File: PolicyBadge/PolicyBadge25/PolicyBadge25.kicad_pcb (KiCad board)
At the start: 2 copper layers, 193.3 x 122.1 mm, 70 parts, among them CN1 PH2.0-2P-LT, J1 Feed Point 915MHz, J2 Feed Point 2.4 GHz, Q1 2N7002, SW1 TA-3525-A1, U1 HS96L03W2C03, U10 YX-SMD5020, U11 IP2312-4V35, U2 MOUDLE-SEEEDUINO-XIAO-ESP32S3, U4 TPS613222ADBVR, U9 TCA9555PWR

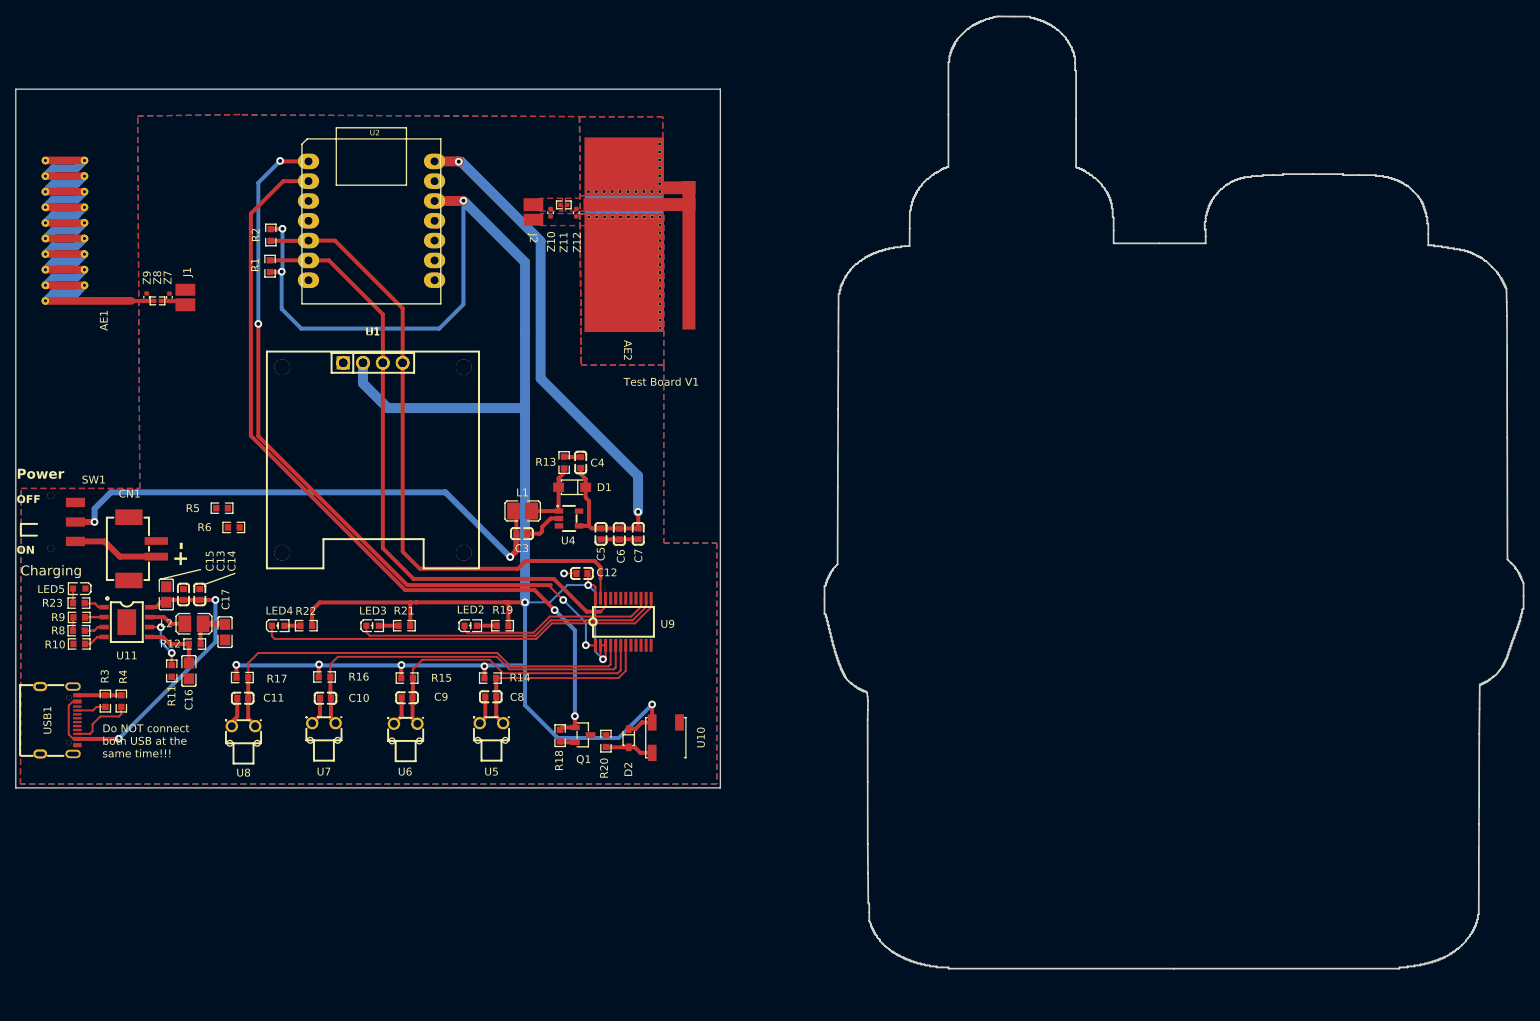
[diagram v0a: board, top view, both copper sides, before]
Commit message: Lots of changes, laying out board for board shape
Updated switches
Added headers for XAIO
Fixed Batt Connector polarity
10K pullup on int
Batt monitor resistor divider
Fix buzzer trace
XAIO footprint spacing
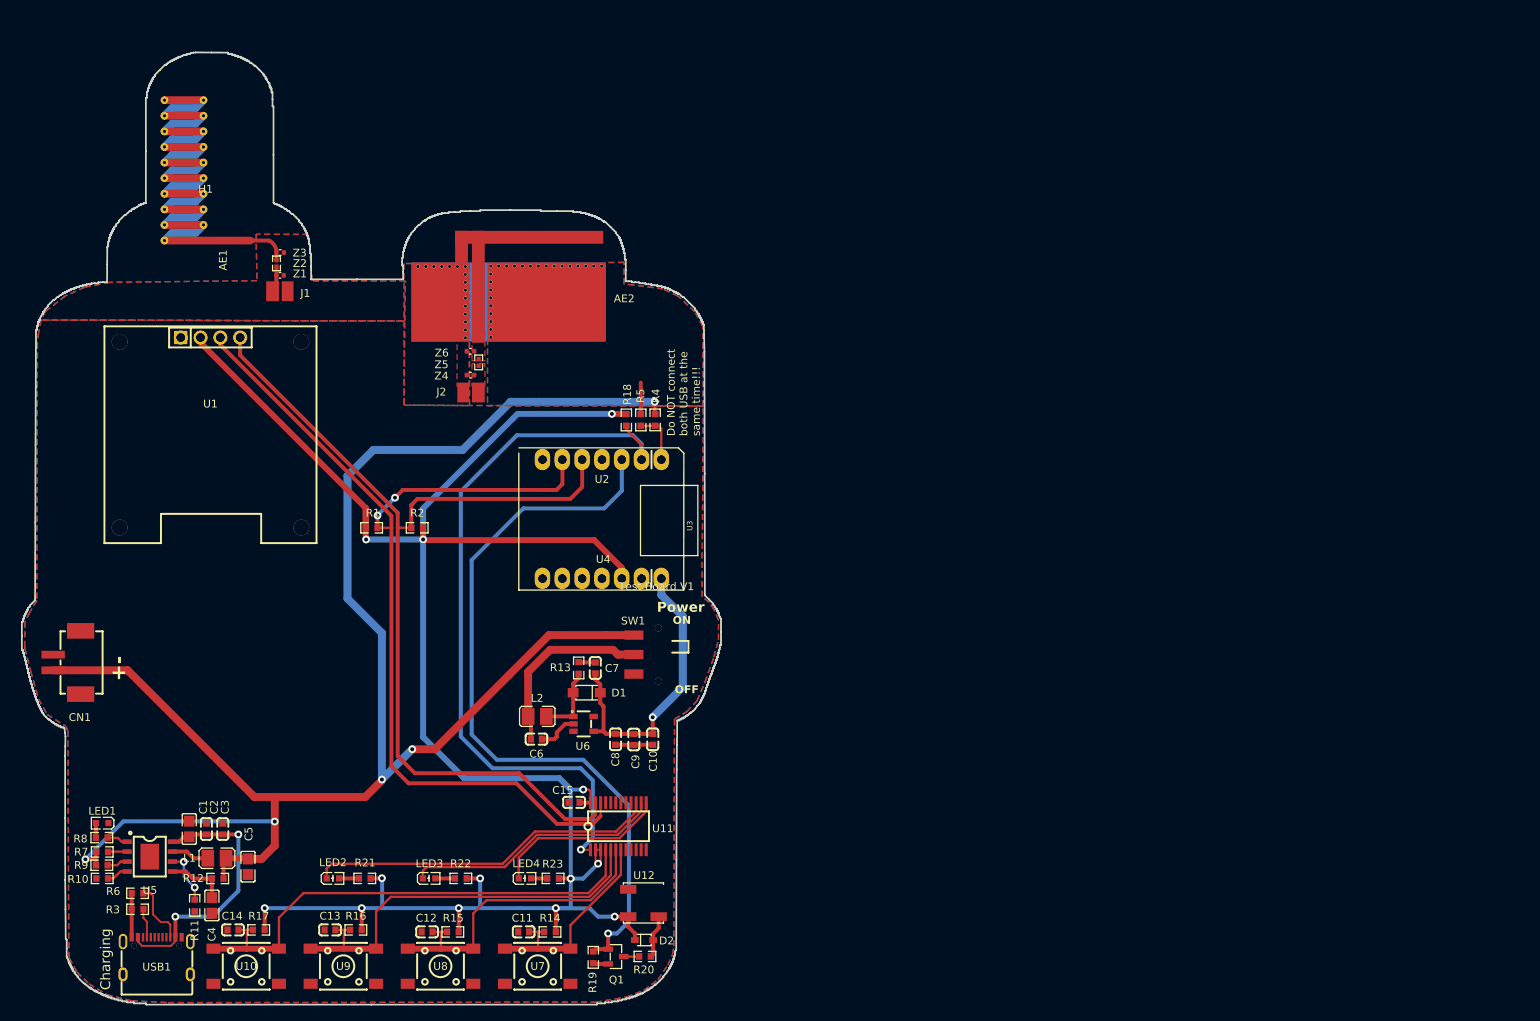
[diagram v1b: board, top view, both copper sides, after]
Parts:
- removed the U5 at (145.8, 120.1)
- removed the U6 at (134.8, 120.2)
- added R18: 10KΩ, imported:R0603, F.Cu at (163.1, 81.2)
- added U10: ~, imported:SW-SMD_4P-L6.0-W6.0-P4.50-LS9.2, F.Cu at (114.3, 151.3)
- added U2: ~, imported:HDR-TH_7P-P2.54-V-F, F.Cu at (160.0, 86.3)
- added U4: ~, imported:HDR-TH_7P-P2.54-V-F, F.Cu at (160.0, 101.6)
- added U9: ~, imported:SW-SMD_4P-L6.0-W6.0-P4.50-LS9.2, F.Cu at (126.8, 151.3)
- U3: renamed from U2; footprint XAIO ESP32S3:MOUDLE14P-SMD-2.54-21X17.8MM-header -> XAIO ESP32S3:MOUDLE14P-SMD-2.54-21X17.8MM-header-fixed
- U7, U8: footprint imported:SW-TH_HRO_K2-1109DF-EXXW-XX -> imported:SW-SMD_4P-L6.0-W6.0-P4.50-LS9.2
- moved SW1 73.6 mm to (164.1, 111.3), turned to 90 degrees
- moved R4 56.7 mm to (166.8, 81.2), turned to 90 degrees
- moved R5 54.0 mm to (164.9, 81.2), turned to -90 degrees
- moved LED4 45.3 mm to (150.1, 140.0)
- moved R23 45.3 mm to (153.7, 140.0)
- moved R2 42.0 mm to (136.3, 95.0), turned to 0 degrees
- moved U7 41.5 mm to (151.7, 151.3), turned to 180 degrees
- moved U8 39.8 mm to (139.3, 151.3), turned to 180 degrees
- moved LED2 36.9 mm to (125.5, 140.0)
- moved R21 36.9 mm to (129.6, 140.0)
- moved R1 36.0 mm to (130.4, 95.0), turned to 180 degrees
- moved U3 34.0 mm to (149.5, 85.5), turned to -90 degrees
- moved R14 33.4 mm to (153.3, 146.9), turned to 180 degrees
- moved LED3 33.2 mm to (137.8, 140.0)
- moved R22 33.2 mm to (141.9, 140.0)
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- renumbered C15 to C1, C7 to C10, C8 to C11, C9 to C12, C10 to C13, C11 to C14, C12 to C15, C13 to C2, C14 to C3, C16 to C4, C17 to C5, C3 to C6, C4 to C7, C5 to C8, C6 to C9, L2 to L1, L1 to L2, LED5 to LED1, R18 to R19, R19 to R21, R21 to R22, R22 to R23, R5 to R4, R6 to R5, R4 to R6, R9 to R7, R23 to R8, R8 to R9, U9 to U11, U10 to U12, U11 to U5, U4 to U6, Z7 to Z1, Z8 to Z2, Z9 to Z3, Z10 to Z4, Z11 to Z5, Z12 to Z6
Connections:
- C11 pad 2: Net-(U9-P03) -> Net-(U11-P03)
- C12 pad 2: Net-(U9-P02) -> Net-(U11-P02)
- C13 pad 2: Net-(U9-P01) -> Net-(U11-P01)
- C14 pad 2: Net-(U9-P00) -> Net-(U11-P00)
- CN1 pad 1: VBATT+ -> GND
- CN1 pad 2: GND -> VBATT+
- R14 pad 2: Net-(U9-P03) -> Net-(U11-P03)
- R15 pad 2: Net-(U9-P02) -> Net-(U11-P02)
- R16 pad 2: Net-(U9-P01) -> Net-(U11-P01)
- R17 pad 2: Net-(U9-P00) -> Net-(U11-P00)
- U11 pad 4: Net-(U9-P00) -> Net-(U11-P00)
- U11 pad 5: Net-(U9-P01) -> Net-(U11-P01)
- U11 pad 6: Net-(U9-P02) -> Net-(U11-P02)
- U11 pad 7: Net-(U9-P03) -> Net-(U11-P03)
- U7 pad 2: Net-(U9-P01) -> GND
- U8 pad 2: Net-(U9-P00) -> GND
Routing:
- net VBATT+: track 18.5 -> 220.8 mm, vias 0 -> 5
- net Net-(U11-P00): track 0.00 -> 64.1 mm
- net Net-(U9-P00): track 58.3 -> 0.00 mm
- net Net-(U11-P01): track 0.00 -> 52.7 mm
- net Net-(U9-P01): track 48.4 -> 0.00 mm
- net /SCL: track 80.6 -> 128.0 mm, vias 0 -> 2
- net /VBATT+_SWITCHED: track 68.3 -> 23.8 mm, vias 2 -> 0
- net /SDA: track 82.7 -> 123.6 mm
- net Net-(U11-P02): track 0.00 -> 40.6 mm
- net Net-(U9-P02): track 38.5 -> 0.00 mm
- net /Boost Reg/5V_OUT: track 75.4 -> 38.2 mm, vias 2 -> 1
- net Net-(LED4-K): track 53.0 -> 22.6 mm
- net Net-(U11-P03): track 0.00 -> 27.8 mm
- net Net-(U9-P03): track 26.4 -> 0.00 mm
- net VCC_3V3: track 284.2 -> 262.6 mm, vias 11 -> 13
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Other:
- board size 193.3 x 122.1 mm -> 89.6 x 122.1 mm
